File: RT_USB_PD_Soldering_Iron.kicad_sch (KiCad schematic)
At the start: 66 parts, among them J1 USB_C_Receptacle_USB2.0, J2 35RASMT4BHNTRX, J3 Conn_02x03_Odd_Even, SW1 SW_Push, SW2 SW_Push, U1 MIC5239-3.3YMM, U2 BMI270, U3 USBLC6-4SC6, U4 NCP5623CMUTBG, U5 STM32G431Kxxx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

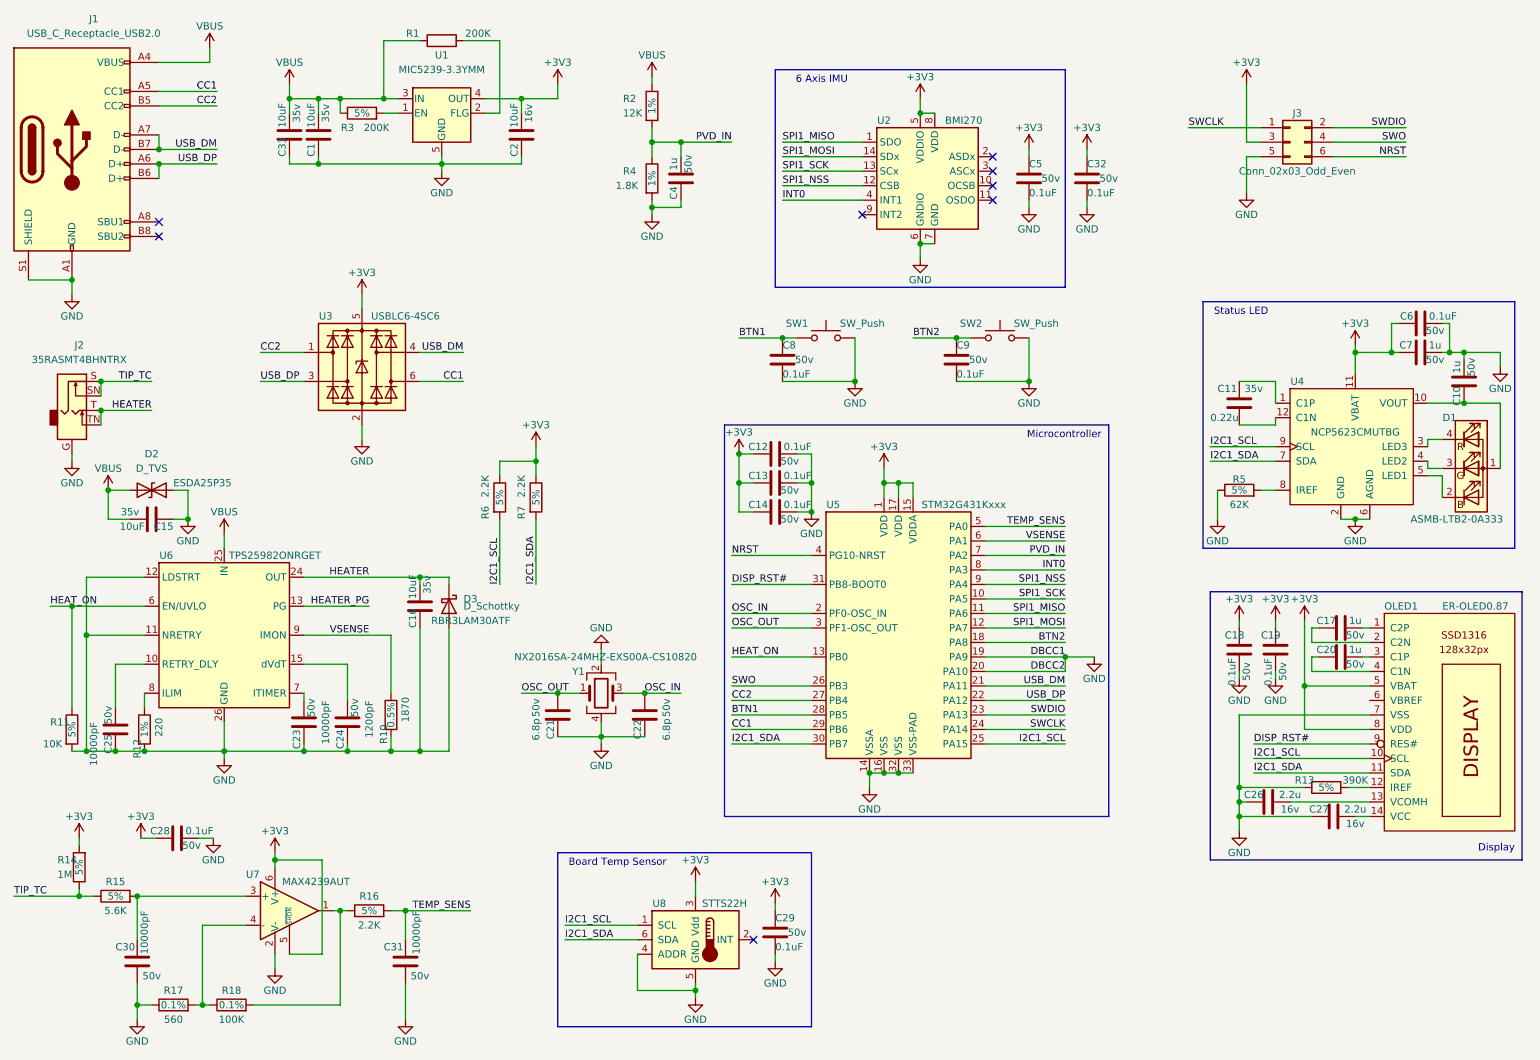
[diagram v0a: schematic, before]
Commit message: New board layout
New layout. Nothing is around the USB connector now. 1mm keepout around the entire board edge. I actually like this layout!
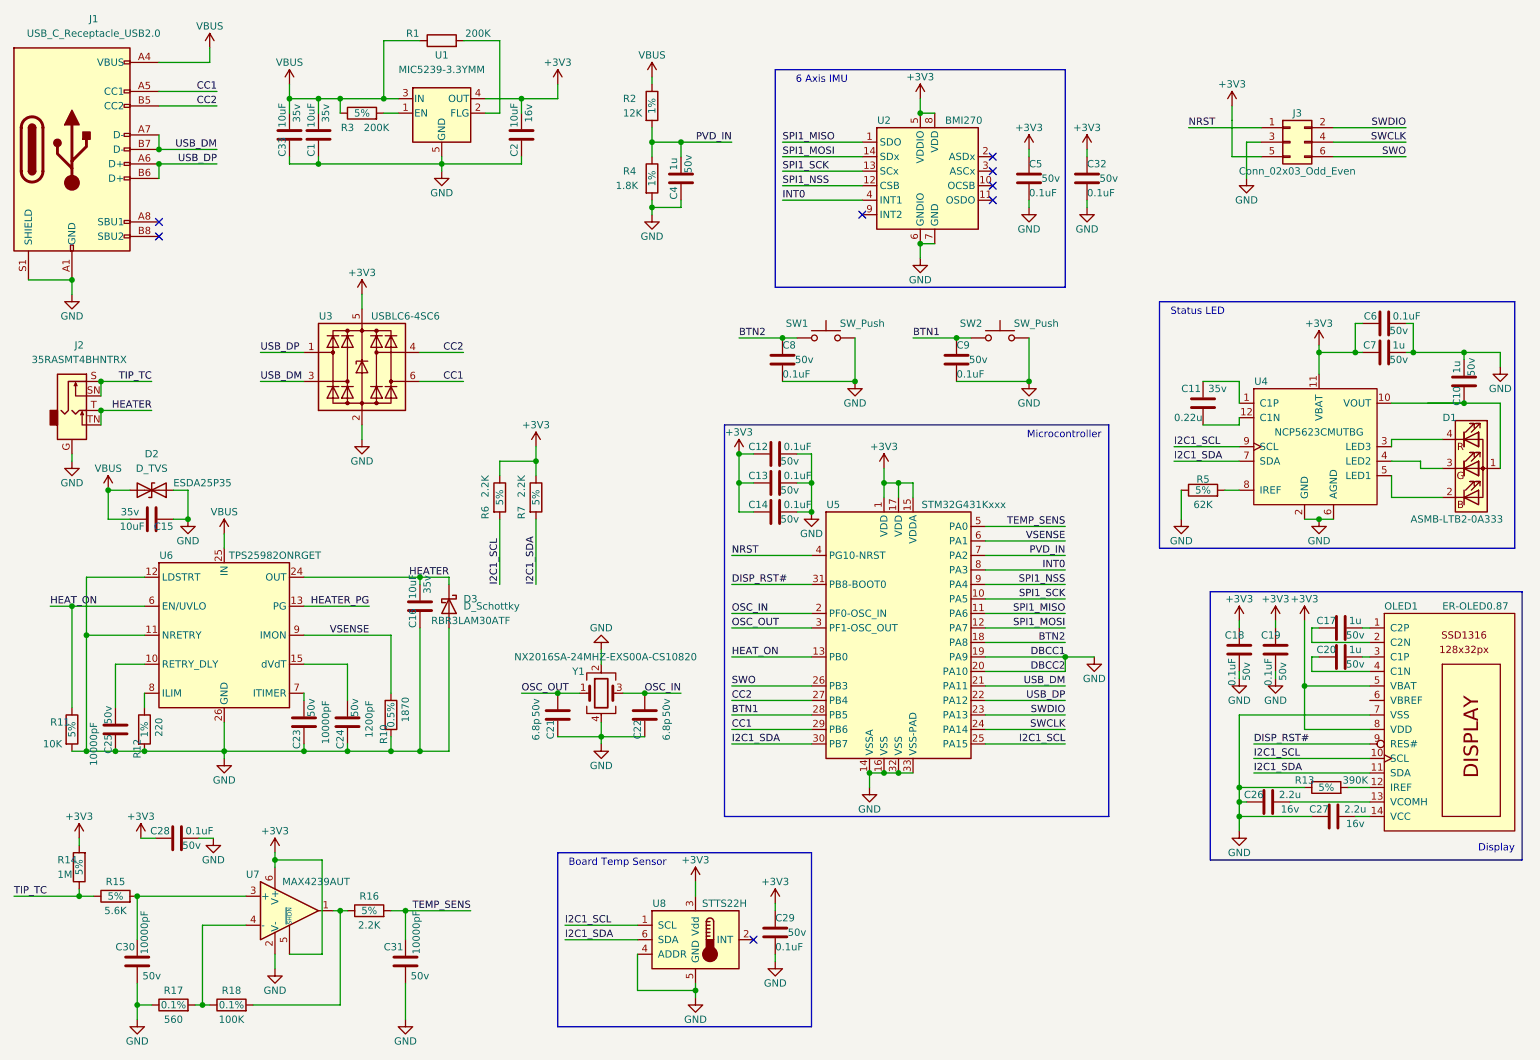
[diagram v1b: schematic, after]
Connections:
- net +3V3: now also J3.5 (Pin_5); no longer J3.3 (Pin_3)
- net BTN1: now also C9.1, SW2.1; no longer C8.1, SW1.1
- net BTN2: now also C8.1, SW1.1; no longer C9.1, SW2.1
- net CC2: now also U3.4 (I/O3); no longer U3.1 (I/O1)
- net GND: now also J3.3 (Pin_3); no longer J3.5 (Pin_5)
- net NRST: now also J3.1 (Pin_1); no longer J3.6 (Pin_6)
- net SWCLK: now also J3.4 (Pin_4); no longer J3.1 (Pin_1)
- net SWO: now also J3.6 (Pin_6); no longer J3.4 (Pin_4)
- net USB_DM: now also U3.3 (I/O2); no longer U3.4 (I/O3)
- net USB_DP: now also U3.1 (I/O1); no longer U3.3 (I/O2)
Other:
- moved on the sheet: C11, C6, C7, R5, U4

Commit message: Update Headphone connector footprint
updating the footprint based on actual measurements.
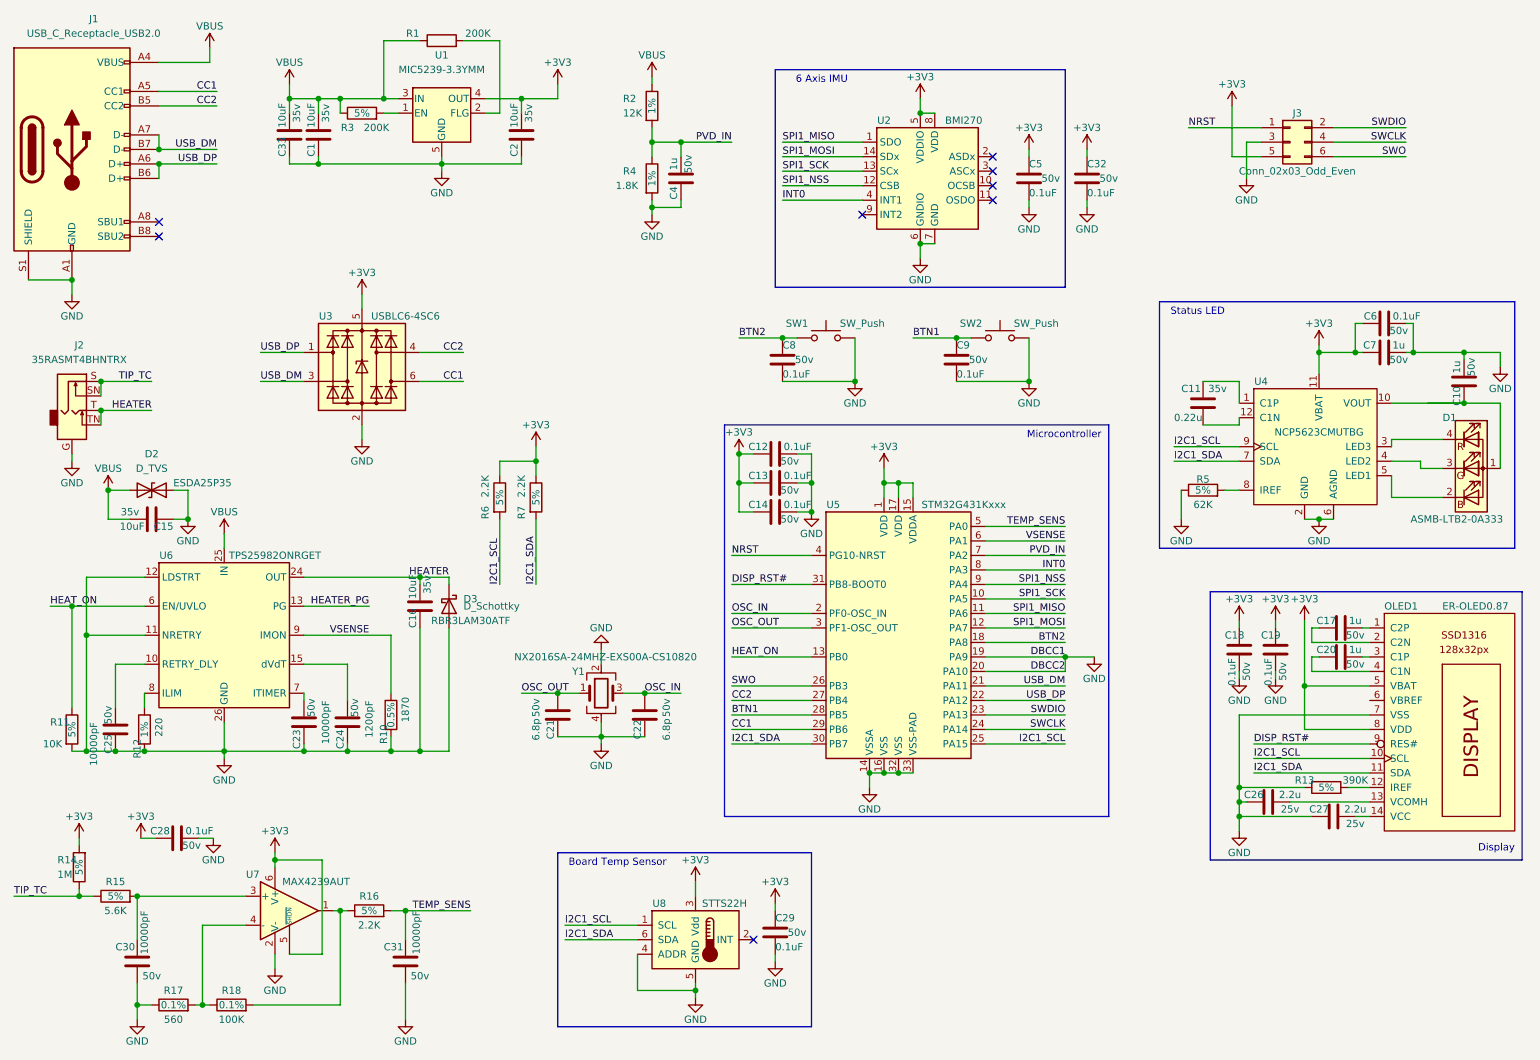
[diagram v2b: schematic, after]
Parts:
- C2: Voltage 16v -> 35v
- C26, C27: Voltage 16v -> 25v
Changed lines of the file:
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@@
   (junction (at 271.78 73.66) (diameter 1.016) (color 0 0 0 0))
   (junction (at 271.78 82.55) (diameter 1.016) (color 0 0 0 0))
+  (no_connect (at 189.23 46.99))
   (no_connect (at 43.18 53.34))
-  (no_connect (at 189.23 46.99))
+  (no_connect (at 147.32 176.53))
+  (no_connect (at 189.23 39.37))
   (no_connect (at 166.37 49.53))
   (no_connect (at 189.23 41.91))
   (no_connect (at 189.23 44.45))
   (no_connect (at 43.18 50.8))
-  (no_connect (at 189.23 39.37))
-  (no_connect (at 147.32 176.53))
   (wire (pts (xy 17.78 168.91) (xy 29.21 168.91))
     (stroke (width 0) (type solid) (color 0 0 0 0))
@@
     (stroke (width 0) (type solid) (color 0 0 0 0))
   )
-  (wire (pts (xy 231.14 30.48) (xy 231.14 33.02))
-    (stroke (width 0) (type solid) (color 0 0 0 0))
-  )
-  (wire (pts (xy 231.14 39.37) (xy 231.14 33.02))
+  (wire (pts (xy 231.14 30.48) (xy 231.14 39.37))
     (stroke (width 0) (type solid) (color 0 0 0 0))
   )
@@
       (effects (font (size 1.27 1.27)) hide)
     )
-    (property "Voltage" "16v" (id 4) (at 107.95 31.75 90))
+    (property "Voltage" "35v" (id 4) (at 107.95 31.75 90))
   )
   (symbol (lib_id "Device:C") (at 113.03 137.16 180) (unit 1)
@@
       (effects (font (size 1.27 1.27)) hide)
     )
-    (property "Voltage" "16v" (id 4) (at 241.3 153.67 90))
+    (property "Voltage" "25v" (id 4) (at 241.3 153.67 90))
   )
   (symbol (lib_id "Device:C") (at 238.76 125.73 0) (unit 1)
@@
       (effects (font (size 1.27 1.27)) hide)
     )
-    (property "Voltage" "16v" (id 4) (at 252.73 156.21 90))
+    (property "Voltage" "25v" (id 4) (at 252.73 156.21 90))
   )
   (symbol (lib_id "Device:C") (at 250.19 121.92 90) (unit 1)

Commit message: Removed LED and reduced size to 80mm
Shortest!
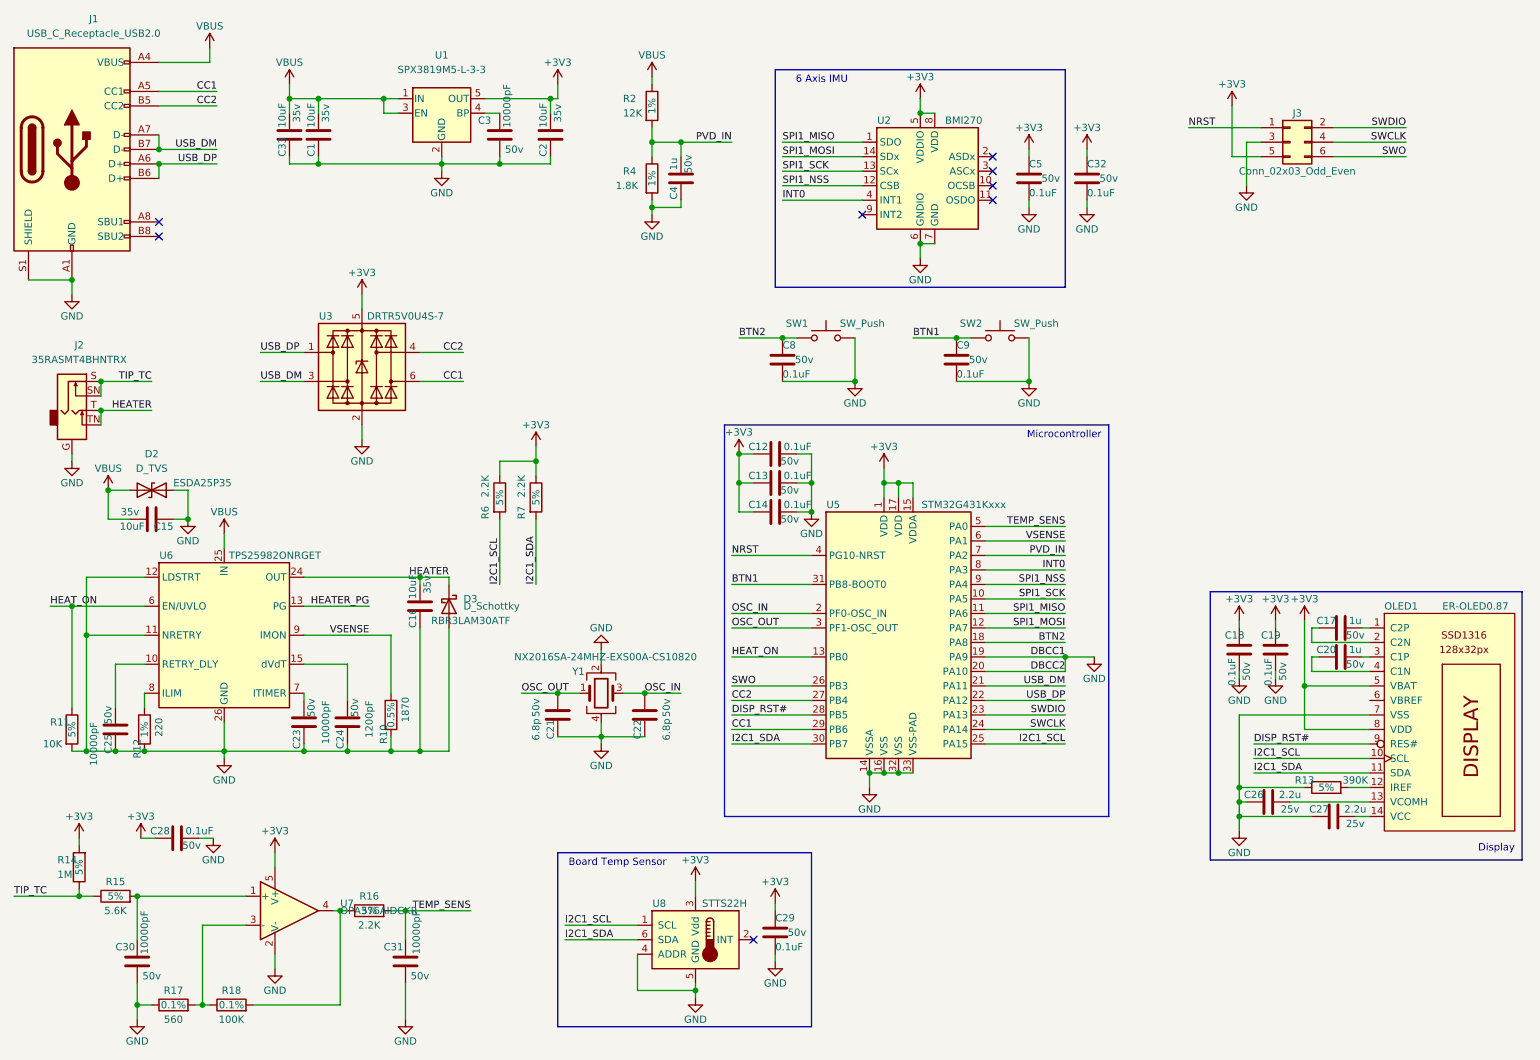
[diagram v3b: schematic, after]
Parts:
- removed C10, C7: 1u, Capacitor_SMD:C_0402_1005Metric, symbol Device:C
- removed C11: 0.22u, Capacitor_SMD:C_0402_1005Metric, symbol Device:C
- removed C6: 0.1uF, Capacitor_SMD:C_0402_1005Metric, symbol Device:C
- removed D1: ASMB-LTB2-0A333, LED_ASMB:LED_SK6805_PLCC4_2.4x2.7mm_P1.3mm, symbol Device:LED_ABGR
- removed R1, R3: 200K, Resistor_SMD:R_0402_1005Metric, symbol Device:R
- removed R5: 62K, Resistor_SMD:R_0402_1005Metric, symbol Device:R
- removed U1: MIC5239-3.3YMM, Package_SO:MSOP-8_3x3mm_P0.65mm, symbol MIC5239-3.0YMM:MIC5239-3.3YMM
- removed U4: NCP5623CMUTBG, LLGA12:LGA-12_2x2mm_P0.5mm, symbol NCP5623C:NCP5623CMUTBG
- removed U7: MAX4239AUT, Package_TO_SOT_SMD:SOT-23-6, symbol Amplifier_Operational:MAX4239AUT
- added C3: 10000pF, Capacitor_SMD:C_0402_1005Metric, symbol Device:C
- added U1: SPX3819M5-L-3-3, Package_TO_SOT_SMD:SOT-23-5, symbol Regulator_Linear:SPX3819M5-L-3-3
- added U7: OPA376AIDCKR, Package_TO_SOT_SMD:SOT-353_SC-70-5, symbol Amplifier_Operational:OPA376xxDCK
- J3: footprint Connector_PinHeader_1.27mm:PinHeader_2x03_P1.27mm_Vertical_SMD -> TE FPC:TE_CONN_FFC_VERT_6POS_0.50MM_SMD
- U3: value USBLC6-4SC6 -> DRTR5V0U4S-7; footprint Package_TO_SOT_SMD:SOT-23-6 -> Package_TO_SOT_SMD:SOT-363_SC-70-6
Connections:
- net +3V3: now also U1.5 (OUT), U7.5 (V+)
- net BTN1: now also U5.31 (PB8-BOOT0); no longer U5.28 (PB5)
- net DISP_RST#: now also U5.28 (PB5); no longer U5.31 (PB8-BOOT0)
- net GND: now also C3.2, U1.2 (GND), U7.2 (V-)
- net IN: now also U1.1 (IN), U1.3 (EN)
- net at C30.1, R15.2: now also U7.1 (+)
- net at R16.1, R18.2: now also U7.4
- net at R17.2, R18.1: now also U7.3 (-)
- new net: C3.1, U1.4 (BP)
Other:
- note removed: "Status LED"
- moved on the sheet: C2

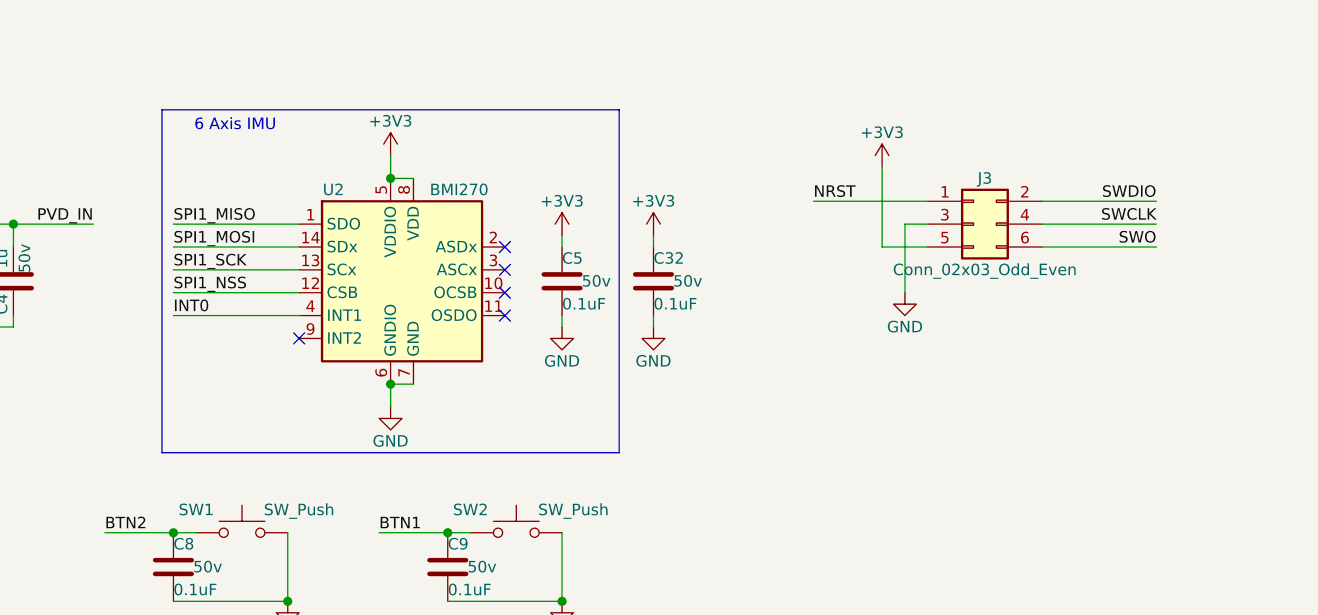
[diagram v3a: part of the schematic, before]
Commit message: Reduce board to 75mm length
Knocked off another 5mm
modified USB connector pads. Increased connector board edge to meet 1mm overhang.
Replaced a few components with new ones (smaller, lower cost).
VReg, Usb ESD protection, and Op-AMP.
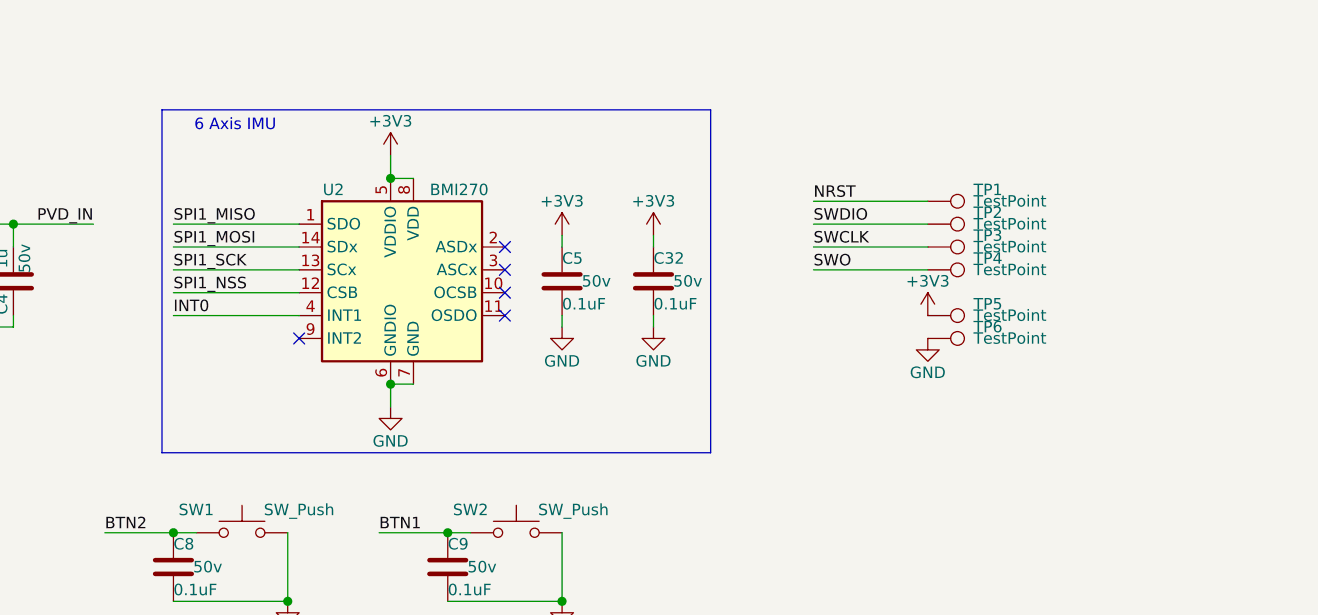
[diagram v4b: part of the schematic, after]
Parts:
- removed J3: Conn_02x03_Odd_Even, TE FPC:TE_CONN_FFC_VERT_6POS_0.50MM_SMD, symbol Connector_Generic:Conn_02x03_Odd_Even
- added TP1, TP2, TP3, TP4, TP5, TP6: TestPoint, TestPoint:TestPoint_Pad_D1.0mm, symbol Connector:TestPoint
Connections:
- net +3V3: now also TP5.1
- net GND: now also TP6.1
- net NRST: now also TP1.1
- net SWCLK: now also TP3.1
- net SWDIO: now also TP2.1
- net SWO: now also TP4.1
